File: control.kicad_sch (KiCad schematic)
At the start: 4 parts

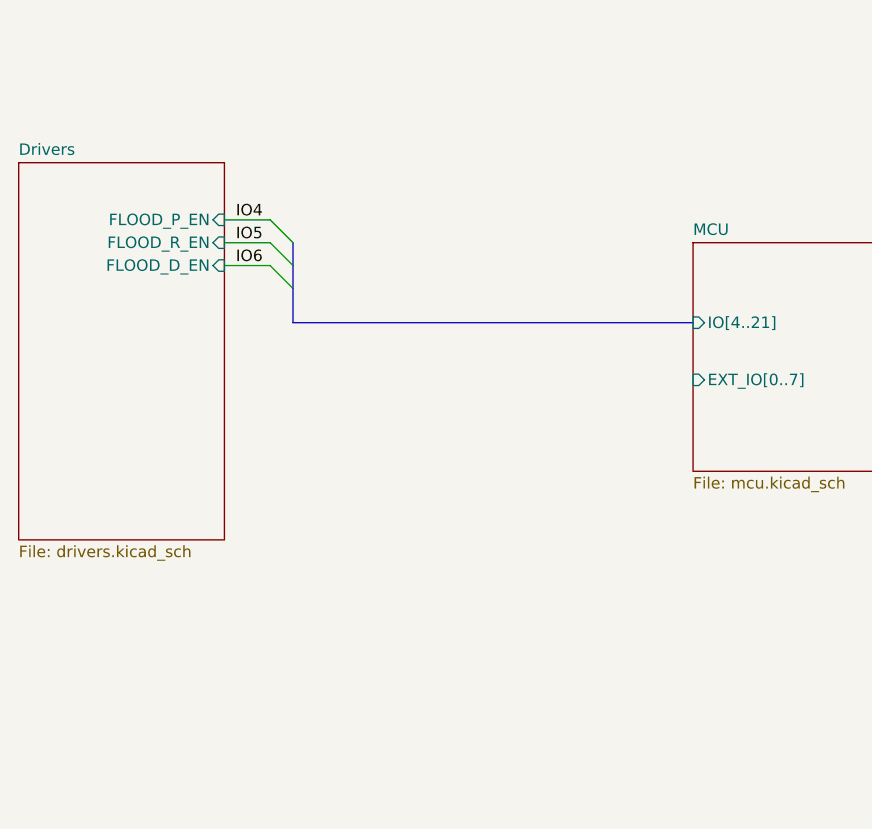
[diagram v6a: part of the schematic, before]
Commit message: add truck drivers
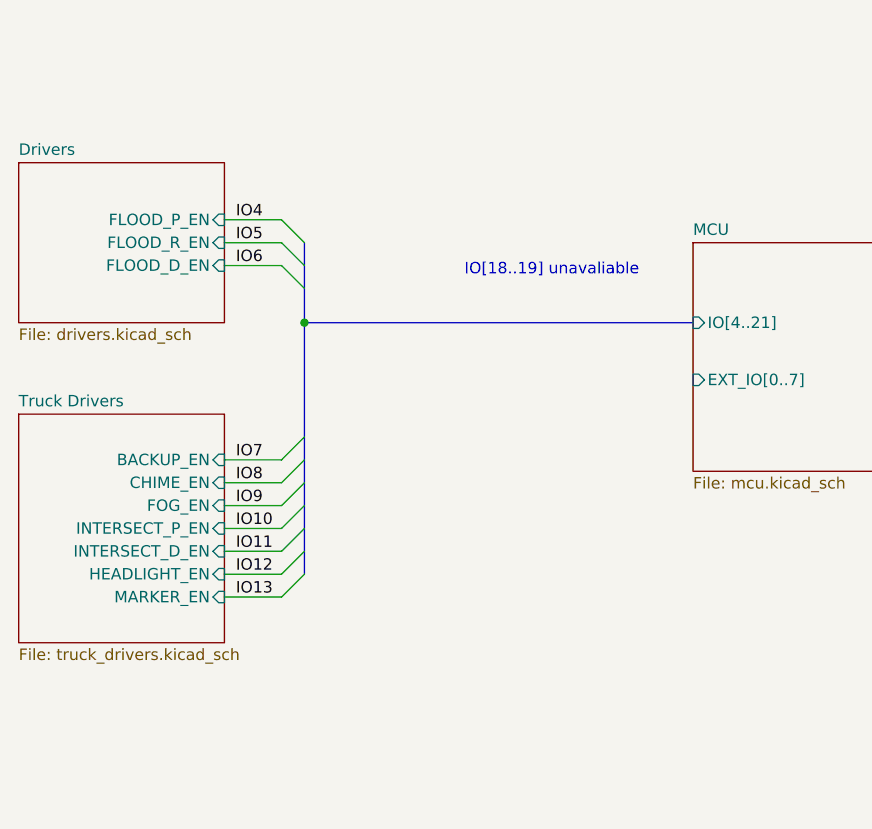
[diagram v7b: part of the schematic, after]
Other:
- added sheet Truck Drivers (truck_drivers.kicad_sch)
- note added: "IO[18..19] unavaliable"

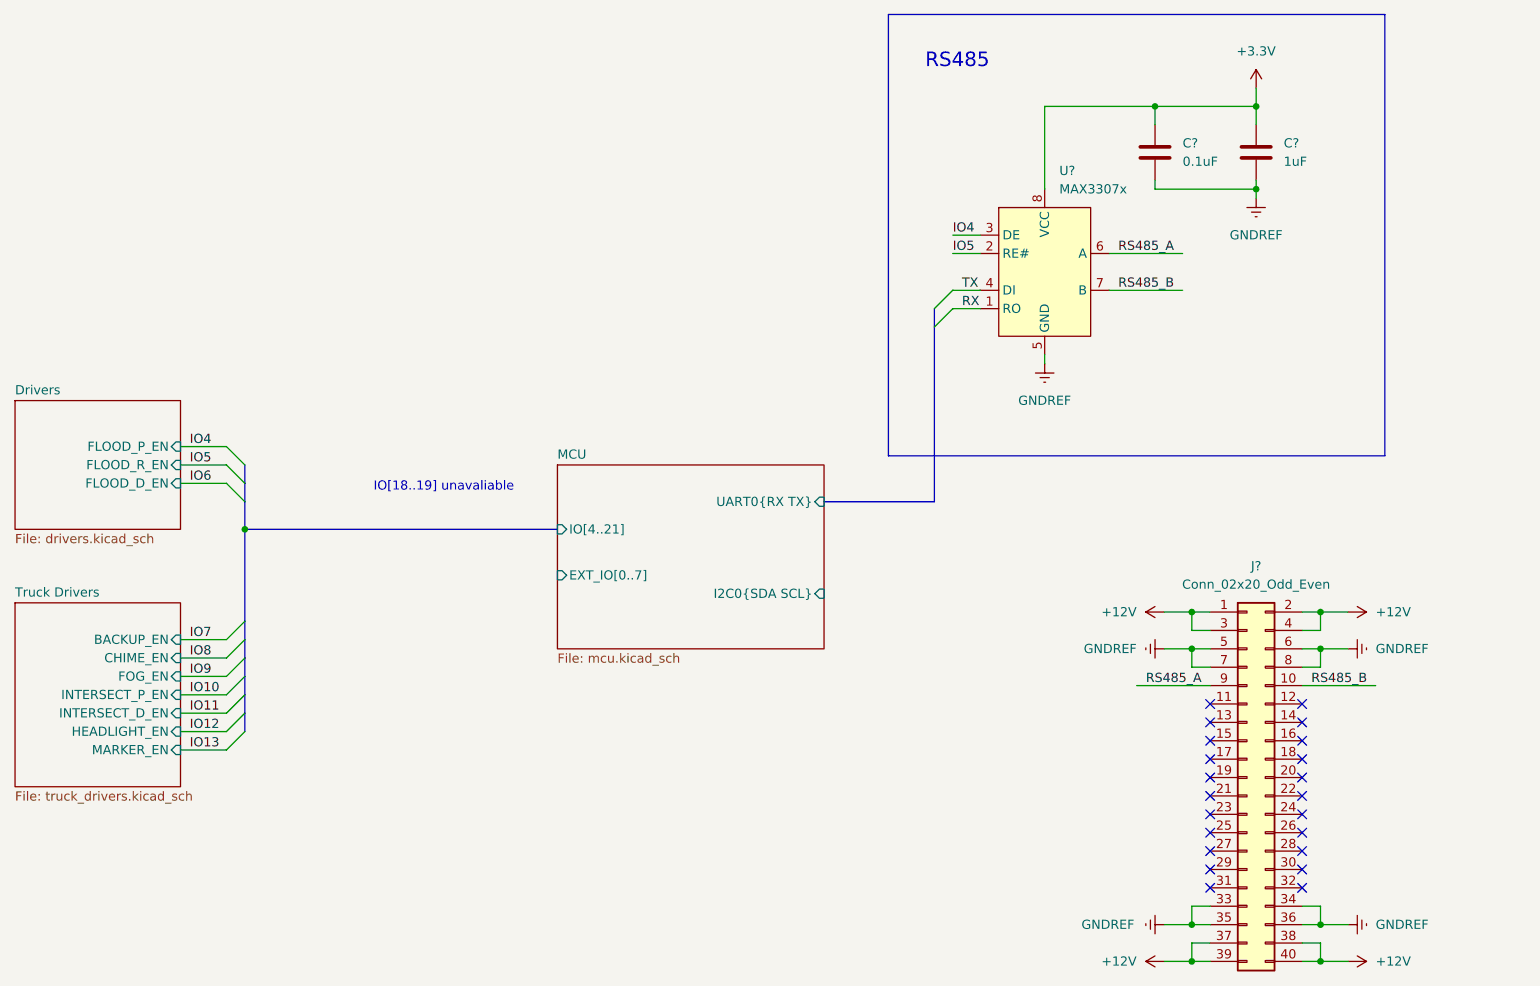
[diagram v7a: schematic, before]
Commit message: add Faston connectors for RS485
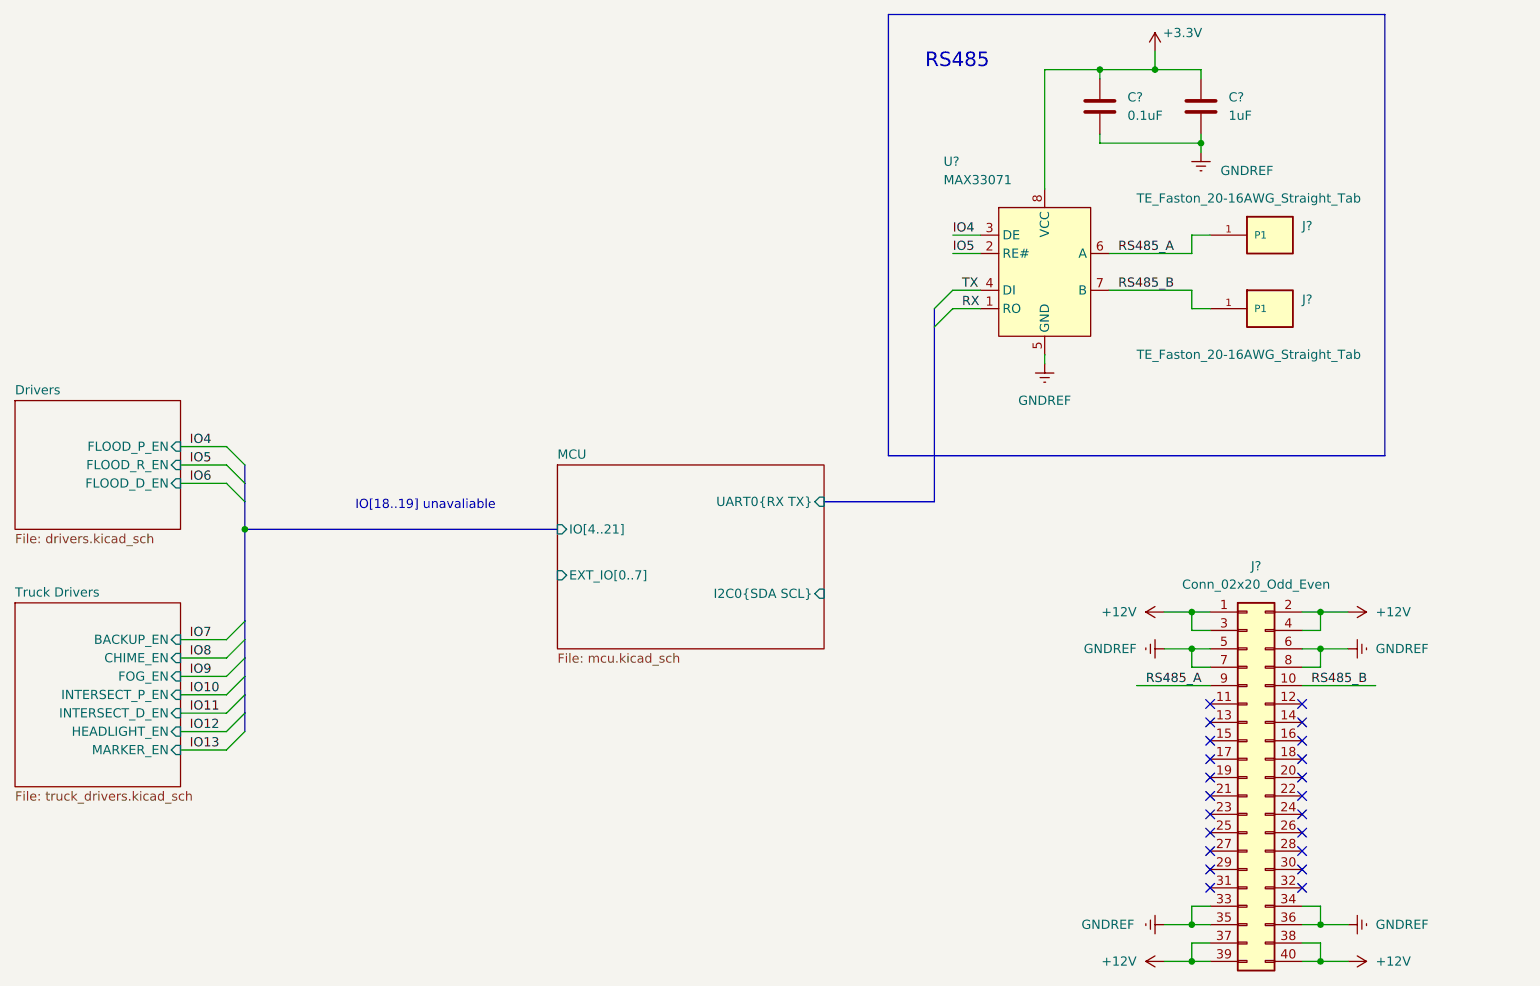
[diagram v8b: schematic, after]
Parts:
- added J? (x2): TE_Faston_20-16AWG_Straight_Tab, TE_Faston_20-16AWG_Straight_Tab, symbol Toadly:TE_Faston_20-16AWG_Straight_Tab
- U?: value MAX3307x -> MAX33071
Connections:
- net RS485_A: now also J?.1 (P1), J?.2 (P1)
- net RS485_B: now also J?.1 (P1), J?.2 (P1)
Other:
- moved on the sheet: C?
